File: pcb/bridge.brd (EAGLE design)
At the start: 99.4 x 59 mm, 37 parts, among them IC1 MEGA8-AI, IC4 78L05SMD, IC5 LM358D

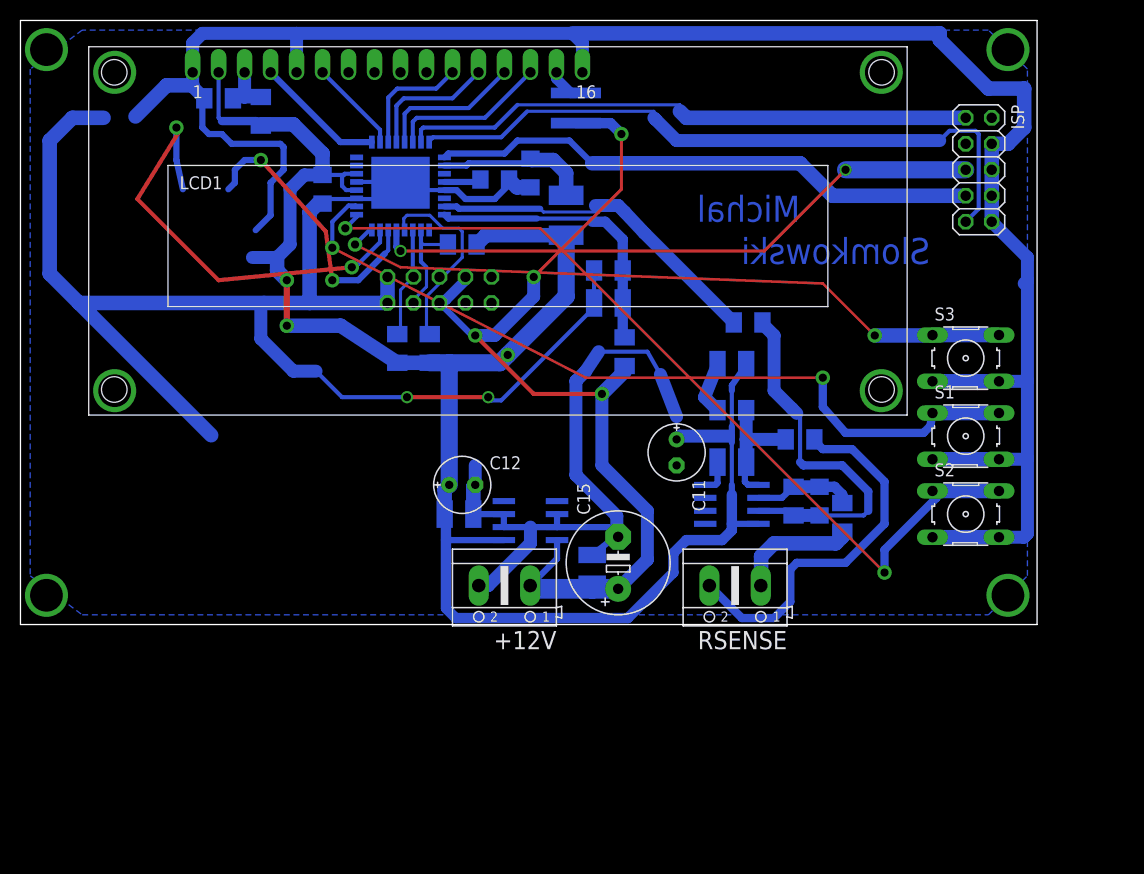
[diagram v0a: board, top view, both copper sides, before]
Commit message: Bridge USB schematic.
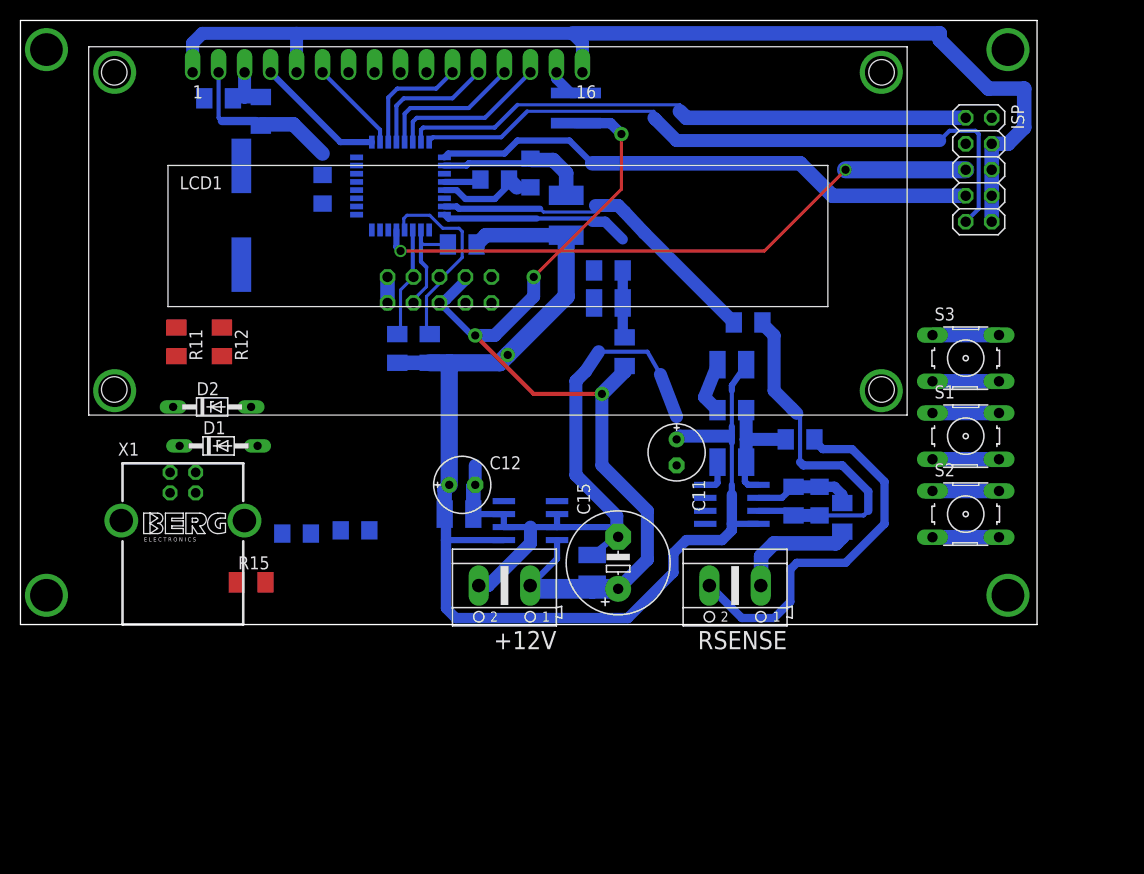
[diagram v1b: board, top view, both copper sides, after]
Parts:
- added C5, C6: 22p, rcl:C1206
- added D1, D2: 3V6, diode:DO34Z7
- added Q1: 16MHz, crystal:HC49UP
- added R11, R12: 68, rcl:M1206
- added R15: 1k5, rcl:M1206
- added X1: PN61729-S, con-berg:PN61729-S
- R3: value 1k -> 2k2
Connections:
- new net FDFDS: S1.1, S1.2
- new net N$11: C5.1, IC1.8, Q1.1
- new net N$5: D2.C, R11.2, R15.1, X1.2
- new net N$6: D1.C, R12.2, X1.3
- new net N$9: C6.1, IC1.7, Q1.2
- new net XXFDSF: S2.1, S2.2
- new net XXX: S3.1, S3.2
- net +5V: now also R15.2
- net GND: now also C5.2, C6.2, D1.A, D2.A, X1.4, X1.S1, X1.S2
- net PD2: no longer S3.1, S3.2
- net PD3: now also R11.1; no longer S2.1, S2.2
- net PD4: now also R12.1; no longer S1.1, S1.2
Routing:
- net GND: track 432.2 -> 215.3 mm, vias 2 -> 0
- net PD3: track 85.2 -> 0.00 mm, vias 2 -> 0
- net PD4: track 79.2 -> 0.00 mm, vias 2 -> 0
- net PD2: track 67.9 -> 0.00 mm, vias 2 -> 0
- net PD1: track 43.7 -> 0.00 mm, vias 2 -> 0
- net +5V: track 179.1 -> 138.3 mm, vias 3 -> 1
- net PD0: track 28.0 -> 0.00 mm, vias 2 -> 0
- net XXX: track 0.00 -> 6.50 mm
- net XXFDSF: track 0.00 -> 6.50 mm
- net FDFDS: track 0.00 -> 6.50 mm
- net PC1: track 28.3 -> 25.2 mm
- net N$10: track 14.9 -> 14.1 mm
- removed copper zone on layer 16, net GND
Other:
- board text removed: "Michal"
- board text removed: "Slomkowski"

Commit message: Bridge board ready.
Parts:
- removed C17: 100n, rcl:C1210
- added C7: 100n, rcl:C1206
- R4: device rcl:R1218 -> rcl:0207/12
- moved R1 56.1 mm to (70.5, 4.76), turned to 90 degrees
- moved R3 48.0 mm to (62.2, 16.8), turned to 90 degrees
- moved BUS 47.9 mm to (57.5, 11.1), flipped to the top
- moved C11 44.6 mm to (21.3, 13.7)
- moved C15 43.2 mm to (14.3, 7.94)
- moved R6 37.7 mm to (86.4, 4.76), turned to 90 degrees
- moved C12 37.6 mm to (69.2, 14.0), turned to 180 degrees
- moved R8 37.5 mm to (85.1, 10.8), turned to 0 degrees
- moved X1 37.4 mm to (41.3, 9.84)
- moved R14 37.1 mm to (47.9, 18.7)
- moved C14 36.2 mm to (19.4, 7.94)
- moved S3 34.8 mm to (94.6, 13.0)
- moved R13 32.2 mm to (50.8, 15.6), turned to 180 degrees
- moved R2 30.3 mm to (52.1, 25.7), turned to 180 degrees
- moved R11 27.9 mm to (32.4, 32.1), flipped to the bottom
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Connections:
- removed net FDFDS: S1.1, S1.2
- removed net XXFDSF: S2.1, S2.2
- removed net XXX: S3.1, S3.2
- net GND: now also C7.2; no longer C17.2
- net PC1: now also C7.1; no longer C17.1
- net PD0: now also S1.1, S1.2
- net PD1: now also S2.1, S2.2
- net PD2: now also S3.1, S3.2
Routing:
- net GND: track 215.3 -> 113.4 mm, vias 0 -> 2
- net PD2: track 0.00 -> 82.6 mm, vias 0 -> 2
- net PD1: track 0.00 -> 74.2 mm, vias 0 -> 2
- net PD0: track 0.00 -> 68.5 mm, vias 0 -> 2
- net +12V: track 95.4 -> 153.2 mm, vias 4 -> 0
- net PC5: track 19.4 -> 54.9 mm
- net PC3: track 11.8 -> 41.0 mm
- net N$6: track 0.00 -> 25.6 mm
- net N$9: track 0.00 -> 24.6 mm
- net N$29: track 37.1 -> 12.6 mm
- net PC4: track 10.9 -> 35.3 mm
- net N$5: track 0.00 -> 21.8 mm
- net +5V: track 138.3 -> 157.3 mm, vias 1 -> 4
- net N$11: track 0.00 -> 15.6 mm
- net PC0: track 34.3 -> 19.8 mm
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- added copper zone on layer 16, net GND
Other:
- board size 99.4 x 59 mm -> 104.2 x 63.6 mm
- board text added: "Michal"
- board text added: "Slomkowski"

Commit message: Changed bridge board.
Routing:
- net +5V: track 157.3 -> 157.1 mm, vias 4 -> 6
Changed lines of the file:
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@@
 <wire x1="33.1724" y1="41.205" x2="31.9975" y2="41.205" width="0.4064" layer="16"/>
 <wire x1="31.9975" y1="41.205" x2="31.4325" y2="40.64" width="0.4064" layer="16"/>
-<wire x1="33.1724" y1="39.605" x2="31.8325" y2="39.605" width="0.4064" layer="16"/>
-<wire x1="31.8325" y1="39.605" x2="31.4325" y2="40.005" width="0.4064" layer="16"/>
-<wire x1="31.4325" y1="40.005" x2="31.4325" y2="40.64" width="0.4064" layer="16"/>
+<wire x1="33.1724" y1="39.605" x2="32.15" y2="39.605" width="0.4064" layer="16"/>
+<wire x1="32.15" y1="39.605" x2="31.75" y2="40.005" width="0.4064" layer="16"/>
+<wire x1="31.75" y1="40.005" x2="31.4325" y2="40.64" width="0.4064" layer="16"/>
 <wire x1="31.4325" y1="40.64" x2="29.715" y2="40.64" width="0.8128" layer="16"/>
 <wire x1="29.715" y1="40.64" x2="29.5275" y2="40.4525" width="0.8128" layer="16"/>
@@
 <wire x1="27.4925" y1="22.5425" x2="25.0825" y2="22.5425" width="1.27" layer="16"/>
 <via x="25.0825" y="22.5425" extent="1-16" drill="0.5" shape="octagon"/>
-<wire x1="25.0825" y1="22.5425" x2="58.42" y2="22.5425" width="0.254" layer="1"/>
 <via x="58.42" y="22.5425" extent="1-16" drill="0.5" shape="octagon"/>
 <wire x1="58.42" y1="22.5425" x2="58.42" y2="20.955" width="1.27" layer="16"/>
@@
 <wire x1="22.225" y1="46.5425" x2="22.225" y2="46.355" width="1.4224" layer="16"/>
 <wire x1="19.685" y1="51.1175" x2="19.685" y2="46.355" width="1.4224" layer="16"/>
+<wire x1="25.0825" y1="22.5425" x2="37.7825" y2="22.5425" width="0.254" layer="1"/>
+<via x="37.7825" y="22.5425" extent="1-16" drill="0.5" shape="octagon"/>
+<wire x1="37.7825" y1="22.5425" x2="44.45" y2="22.5425" width="1.27" layer="16"/>
+<via x="44.45" y="22.5425" extent="1-16" drill="0.5" shape="octagon"/>
+<wire x1="44.45" y1="22.5425" x2="58.42" y2="22.5425" width="0.254" layer="1"/>
 </signal>
 <signal name="N$8">

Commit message: Corrected bridge voltage divider to match the resistor values.
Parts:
- R13: value 10k -> 8k2
- R14: value 1k -> 470
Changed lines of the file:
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@@
 <element name="C16" library="rcl" package="C1210" value="100n" x="77.7875" y="20.32" rot="MR270"/>
 <element name="R10" library="rcl" package="M1206" value="100" x="56.1975" y="29.21" rot="MR90"/>
-<element name="R13" library="rcl" package="M1206" value="10k" x="50.8" y="15.5575" rot="MR180"/>
-<element name="R14" library="rcl" package="M1206" value="1k" x="47.9425" y="18.7325" rot="MR180"/>
+<element name="R13" library="rcl" package="M1206" value="8k2" x="50.8" y="15.5575" rot="MR180"/>
+<element name="R14" library="rcl" package="M1206" value="470" x="47.9425" y="18.7325" rot="MR180"/>
 <element name="RSENSE" library="con-ptr500" package="AK500/2" value="" x="78.74" y="6.35" rot="R180">
 <attribute name="MF" value="" x="78.74" y="6.35" size="1.778" layer="27" rot="R180" display="off"/>

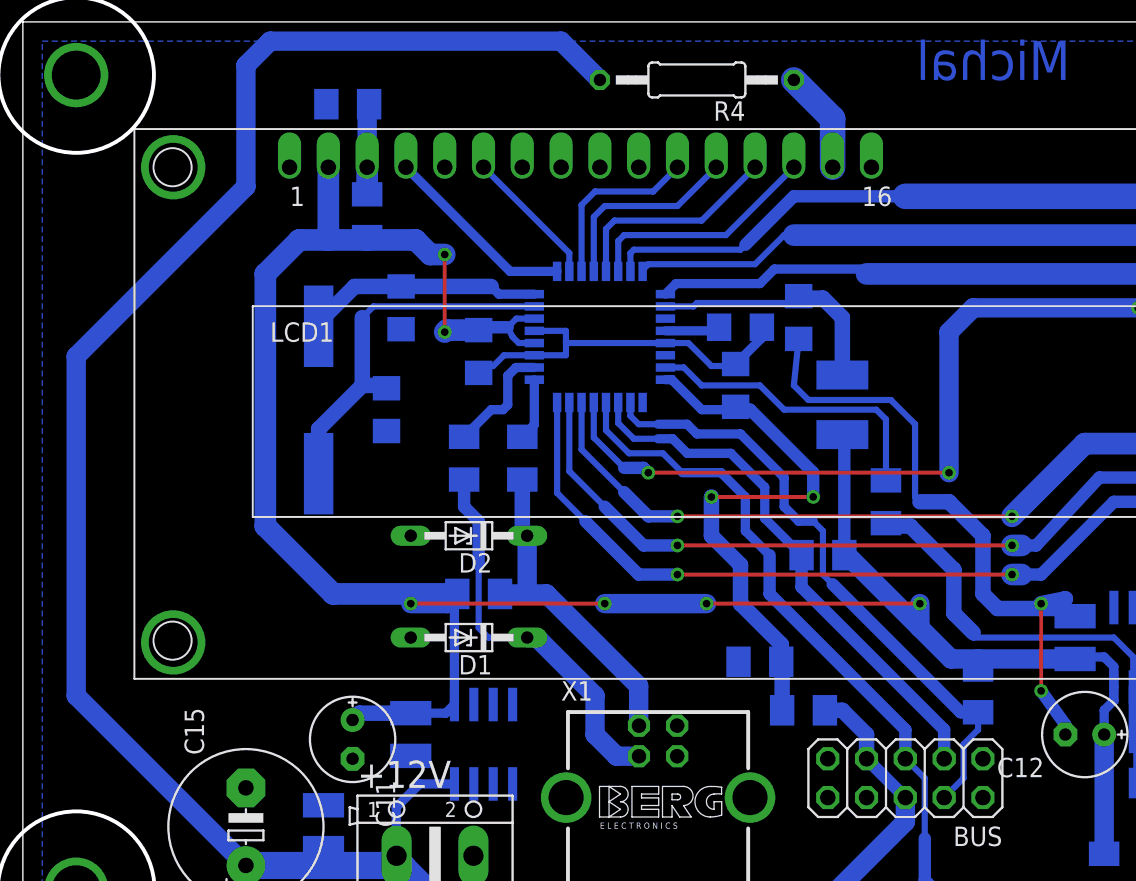
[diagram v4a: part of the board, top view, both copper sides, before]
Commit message: Changed op-amp resistors values on the bridge schematic and general clean-up.
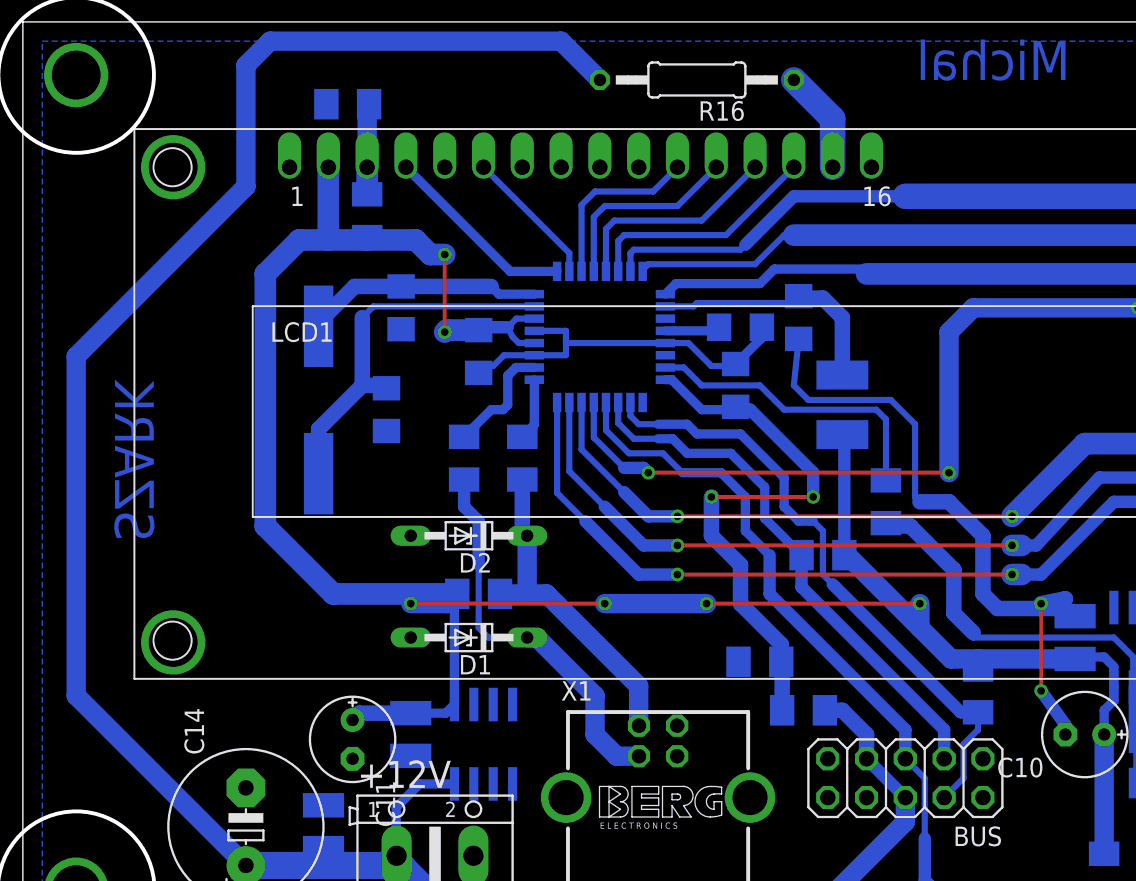
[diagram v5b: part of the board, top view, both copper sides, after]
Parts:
- removed C15: 1000u, rcl:E5-10,5
- removed C16: 100n, rcl:C1210
- added C10: 22u, rcl:E2,5-6E
- added C8: 100n, rcl:C1206
- C1, C2: value 100n -> 22p
- C12: value 22u -> 100n; device rcl:E2,5-6E -> rcl:C1210
- C14: value 100n -> 470u; device rcl:C1210 -> rcl:E5-10,5
- C5, C6: value 22p -> 100n
- C7: device rcl:C1206 -> rcl:C1210
- R1: value 4k7 -> 8k2
- R10: value 100 -> 2k2
- R13: value 8k2 -> 1k5
- R14: value 470 -> 10k
- R15: value 1k5 -> 1k
- R16: value (none) -> 680; device rcl:M1206 -> rcl:0207/12
- R2: value 4k7 -> 470
- R3: value 2k2 -> 8k2
- R4: value (none) -> 10k; device rcl:0207/12 -> rcl:M1206
- R5: value (none) -> 8k2
- R6: value 1k -> 10k
- R7: value 1k -> 100
- R8, R9: value 3k3 -> 4k7
- moved R5 68.4 mm to (79.7, 10.8), turned to 0 degrees
- moved R4 61.8 mm to (85.1, 10.8), flipped to the bottom, turned to 0 degrees
- moved C12 44.1 mm to (25.1, 14.0), flipped to the bottom, turned to 90 degrees
- moved R14 38.9 mm to (22.2, 47.9), turned to 270 degrees
- moved C4 36.5 mm to (50.5, 41.3), turned to 270 degrees
- moved C7 35.5 mm to (77.8, 20.3), turned to 270 degrees
- moved R15 33.2 mm to (21.0, 55.2), turned to 180 degrees
- moved R7 29.9 mm to (56.2, 29.2), turned to 90 degrees
- moved C2 27.7 mm to (23.5, 35.2)
- moved R3 27.0 mm to (86.4, 4.76)
- moved R9 26.8 mm to (52.1, 25.7), turned to 180 degrees
- moved R16 22.9 mm to (43.8, 56.8), flipped to the top
- moved C6 22.9 mm to (46.4, 36.8), turned to 90 degrees
- moved R13 22.6 mm to (29.5, 23.2), turned to 0 degrees
- moved R1 22.5 mm to (50.8, 15.6), turned to 180 degrees
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- renumbered C19 to C9, IC4 to IC3, IC5 to IC2
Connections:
- net +12V: now also C13.2, C14.+, R1.2, R16.2; no longer C14.2, C15.+, R13.2, R4.2
- net +5V: now also C10.+, C12.2, C5.1, R10.2, R13.2, R14.2, R8.2, R9.2; no longer C1.1, C12.+, C13.2, R1.2, R15.2, R2.2, R3.2, R5.2
- net GND: now also C10.-, C12.1, C14.-, C4.2, C7.1, R15.1, R2.1, R4.1; no longer C12.-, C14.1, C15.-, C16.1, C7.2, R14.1, R16.1, R8.1
- net N$1: now also C7.2, R3.2, R4.2; no longer C16.2, R6.2, R8.2
- net N$10: now also C4.1; no longer C2.1
- net N$11: now also C1.1; no longer C5.1
- net N$2: now also R16.1; no longer R4.1
- net N$21: now also R5.1; no longer R7.1
- net N$29: now also R3.1; no longer R6.1
- net N$3: now also R14.1, R15.2; no longer R16.2, R5.1
- net N$4: now also C8.2, R5.2, R6.1; no longer C4.2, R7.2, R9.1
- net N$5: now also R13.1; no longer R15.1
- net N$9: now also C2.1; no longer C6.1
- net NET3: now also C8.1, R6.2, R7.1; no longer C4.1, R10.1, R9.2
- net PC0: now also R7.2; no longer R10.2
- net PC1: now also C6.1, R1.1, R2.2; no longer C7.1, R13.1, R14.2
- net PC3: now also R10.1; no longer R3.1
- net PC4: now also R9.1; no longer R2.1
- net PC5: now also R8.1; no longer R1.1
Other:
- board text added: "SZARK"
